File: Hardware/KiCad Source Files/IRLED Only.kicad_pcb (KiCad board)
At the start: 2 copper layers, 35 x 25 mm, 14 parts

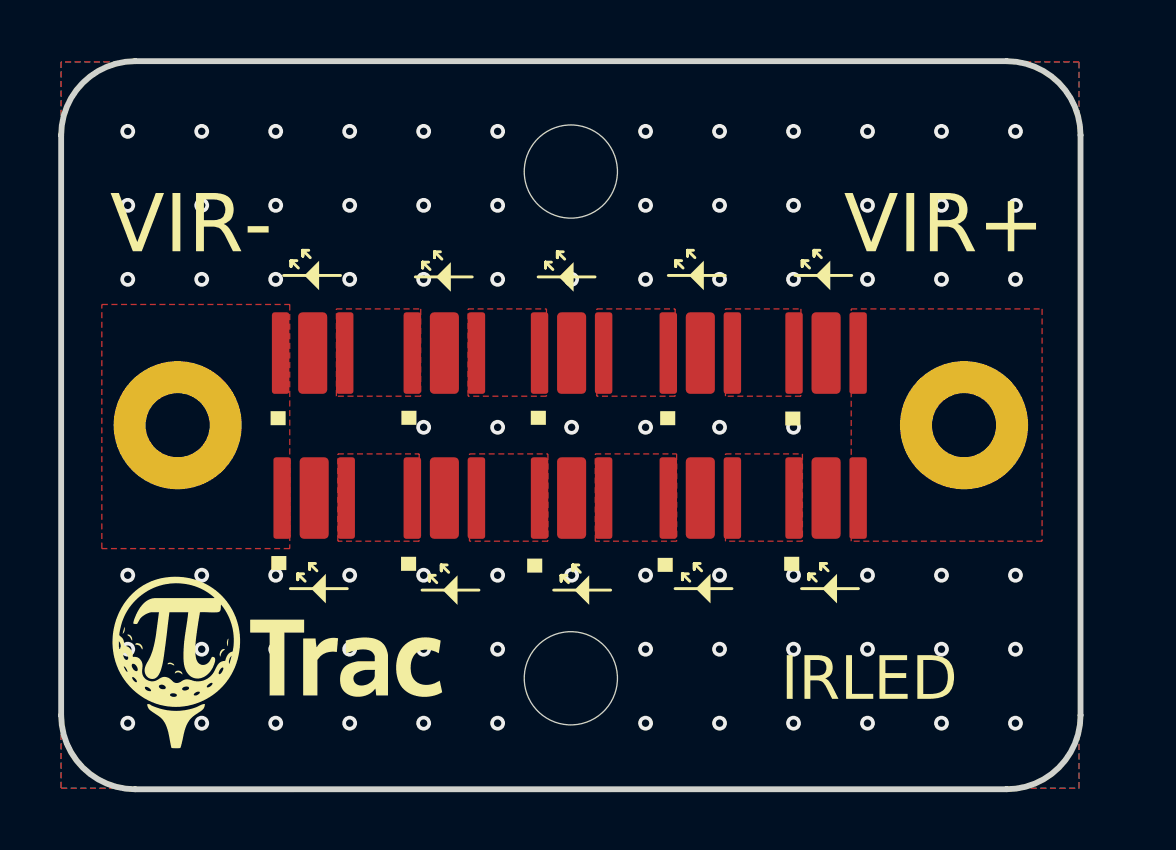
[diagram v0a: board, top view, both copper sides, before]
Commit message: Replace IRLED1 [Original] with IRLED2. Fixes problem supporting cheap IRLED we found right before heading to fabrication.
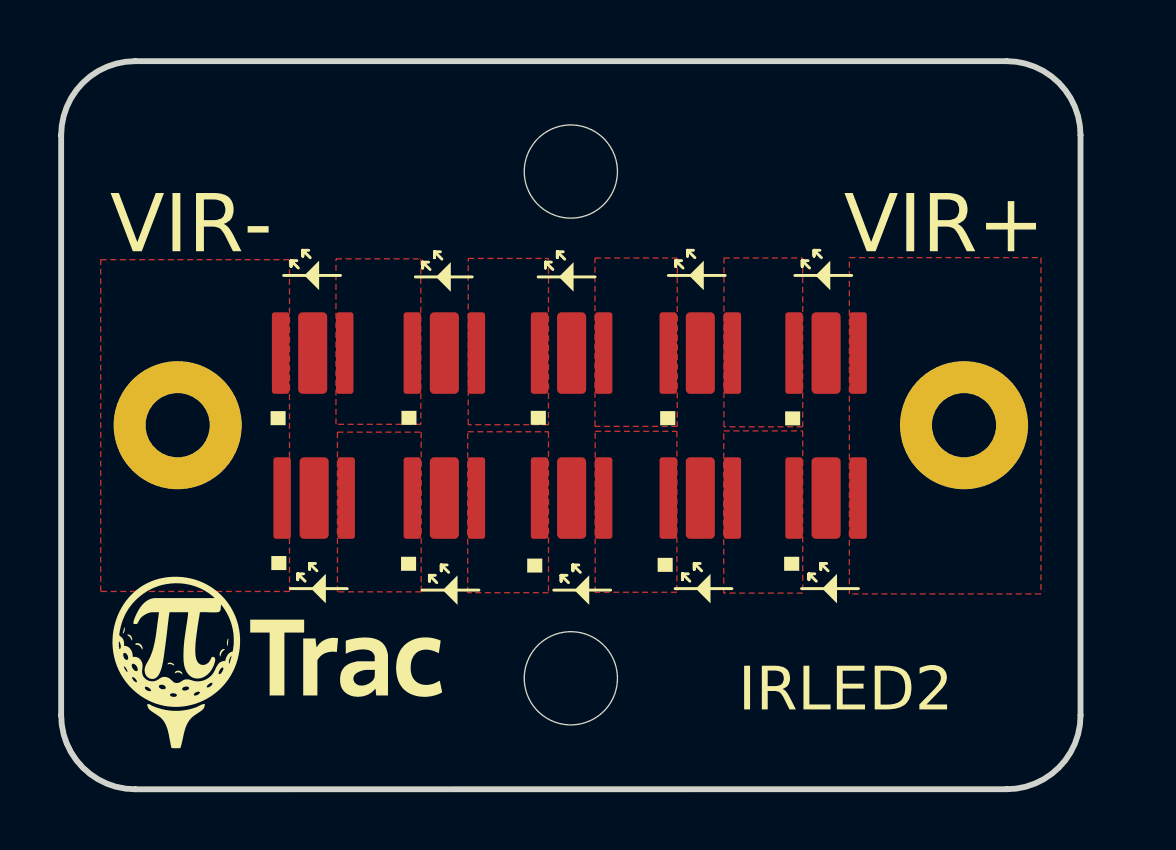
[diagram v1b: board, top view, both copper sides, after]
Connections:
- D10 pad 3: Net-(D10-P) -> (no net)
- D11 pad 3: Net-(D10-P) -> (no net)
- D12 pad 3: Net-(D10-P) -> (no net)
- D13 pad 3: Net-(D10-P) -> (no net)
- D14 pad 3: Net-(D10-P) -> (no net)
- D15 pad 3: Net-(D10-P) -> (no net)
- D6 pad 3: Net-(D10-P) -> (no net)
- D7 pad 3: Net-(D10-P) -> (no net)
- D8 pad 3: Net-(D10-P) -> (no net)
- D9 pad 3: Net-(D10-P) -> (no net)
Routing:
- net Net-(D10-P): vias 80 -> 0
- removed copper zone on B.Cu, net Net-(D10-P)
- removed copper zone on F.Cu, net Net-(D10-P)
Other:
- board text added: "IRLED2"
- board text removed: "IRLED"
